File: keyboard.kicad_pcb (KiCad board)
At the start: 2 copper layers, 359.9 x 94.6 mm, 211 parts, among them IC1 ATMEGA32U4, J1 USB C, X1 ASX3F

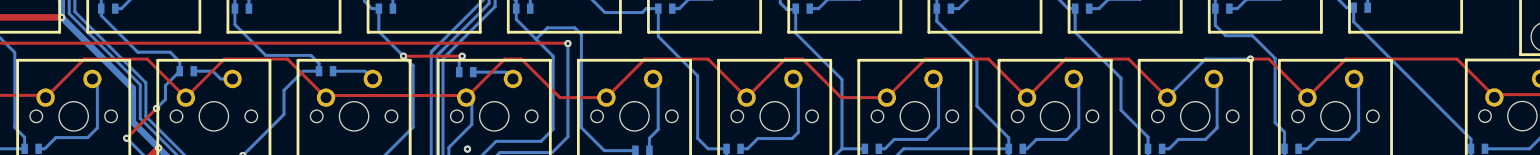
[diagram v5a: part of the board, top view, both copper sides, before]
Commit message: Make fourth row linear
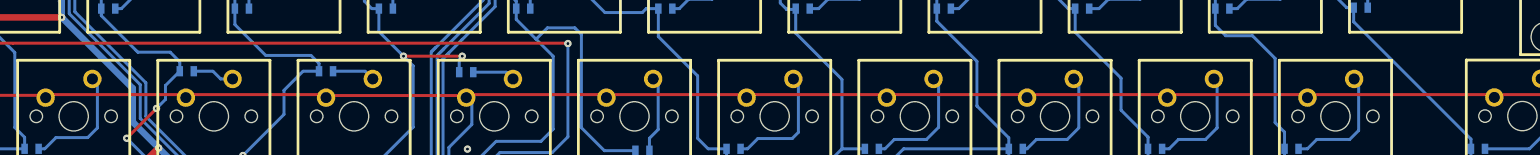
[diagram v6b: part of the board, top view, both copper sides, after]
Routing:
- net /row4: track 410.0 -> 374.6 mm, vias 1 -> 0
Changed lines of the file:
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@@
     (thickness 1.6002)
     (drawings 87)
-    (tracks 1713)
+    (tracks 1718)
     (zones 0)
     (modules 211)
@@
   (layers
     (0 F.Cu signal)
-    (31 B.Cu signal hide)
+    (31 B.Cu signal)
     (32 B.Adhes user hide)
     (33 F.Adhes user hide)
@@
   (segment (start 322.0085 108.966) (end 322.42125 109.37875) (width 0.4064) (layer F.Cu) (net 73))
   (segment (start 291.846 108.966) (end 322.0085 108.966) (width 0.4064) (layer F.Cu) (net 73))
-  (segment (start 191.93002 123.19) (end 186.69 128.43002) (width 0.4064) (layer F.Cu) (net 74))
-  (segment (start 200.49998 123.19) (end 191.93002 123.19) (width 0.4064) (layer F.Cu) (net 74))
-  (segment (start 205.74 128.43002) (end 200.49998 123.19) (width 0.4064) (layer F.Cu) (net 74) (status 10))
-  (segment (start 148.59 128.43002) (end 143.34998 123.19) (width 0.4064) (layer F.Cu) (net 74))
-  (segment (start 124.29998 123.19) (end 115.73002 123.19) (width 0.4064) (layer F.Cu) (net 74))
-  (segment (start 230.03002 123.19) (end 224.79 128.43002) (width 0.4064) (layer F.Cu) (net 74))
-  (segment (start 243.84 128.43002) (end 238.59998 123.19) (width 0.4064) (layer F.Cu) (net 74))
-  (segment (start 238.59998 123.19) (end 230.03002 123.19) (width 0.4064) (layer F.Cu) (net 74))
-  (segment (start 262.89 128.43002) (end 257.64998 123.19) (width 0.4064) (layer F.Cu) (net 74))
-  (segment (start 134.78002 123.19) (end 129.54 128.43002) (width 0.4064) (layer F.Cu) (net 74))
-  (segment (start 129.54 128.43002) (end 124.29998 123.19) (width 0.4064) (layer F.Cu) (net 74))
-  (segment (start 115.73002 123.19) (end 110.49 128.43002) (width 0.4064) (layer F.Cu) (net 74))
-  (segment (start 249.08002 123.19) (end 243.84 128.43002) (width 0.4064) (layer F.Cu) (net 74))
-  (segment (start 143.34998 123.19) (end 134.78002 123.19) (width 0.4064) (layer F.Cu) (net 74))
-  (segment (start 257.64998 123.19) (end 249.08002 123.19) (width 0.4064) (layer F.Cu) (net 74))
-  (segment (start 167.64 128.43002) (end 172.86351 123.20651) (width 0.4064) (layer F.Cu) (net 74))
-  (segment (start 172.86351 123.20651) (end 172.88002 123.19) (width 0.4064) (layer F.Cu) (net 74))
-  (segment (start 180.37302 128.43002) (end 186.69 128.43002) (width 0.4064) (layer F.Cu) (net 74))
-  (segment (start 175.133 123.19) (end 180.37302 128.43002) (width 0.4064) (layer F.Cu) (net 74))
-  (segment (start 172.88002 123.19) (end 175.133 123.19) (width 0.4064) (layer F.Cu) (net 74))
   (segment (start 168.19626 129.18694) (end 167.64 128.43002) (width 0.4064) (layer B.Cu) (net 74))
   (segment (start 78.96225 127.889) (end 79.502 128.42875) (width 0.4064) (layer B.Cu) (net 74))
   (segment (start 79.502 128.42875) (end 79.53375 128.42875) (width 0.4064) (layer B.Cu) (net 74))
-  (segment (start 262.89 128.397) (end 268.097 123.19) (width 0.4064) (layer B.Cu) (net 74))
-  (segment (start 268.097 123.19) (end 274.193 123.19) (width 0.4064) (layer B.Cu) (net 74))
-  (via (at 274.193 123.19) (size 1) (layers F.Cu B.Cu) (net 74))
-  (segment (start 274.193 123.19) (end 276.69998 123.19) (width 0.4064) (layer F.Cu) (net 74))
-  (segment (start 276.69998 123.19) (end 281.94 128.43002) (width 0.4064) (layer F.Cu) (net 74))
   (segment (start 262.89 128.43002) (end 262.89 128.397) (width 0.4064) (layer B.Cu) (net 74))
   (segment (start 167.64 128.43002) (end 168.148 128.93802) (width 0.4064) (layer B.Cu) (net 74))
-  (segment (start 213.36 123.19) (end 218.60002 128.43002) (width 0.4064) (layer F.Cu) (net 74))
-  (segment (start 218.60002 128.43002) (end 224.79 128.43002) (width 0.4064) (layer F.Cu) (net 74))
-  (segment (start 205.74 128.43002) (end 210.98002 123.19) (width 0.4064) (layer F.Cu) (net 74) (status 20))
-  (segment (start 210.98002 123.19) (end 213.36 123.19) (width 0.4064) (layer F.Cu) (net 74))
-  (segment (start 281.94 128.43002) (end 287.18002 123.19) (width 0.4064) (layer F.Cu) (net 74))
-  (segment (start 302.26 123.19) (end 307.34 128.27) (width 0.4064) (layer F.Cu) (net 74))
-  (segment (start 287.18002 123.19) (end 302.26 123.19) (width 0.4064) (layer F.Cu) (net 74))
   (segment (start 307.975 127.635) (end 307.34 128.27) (width 0.4064) (layer F.Cu) (net 74))
   (segment (start 332.74 127.635) (end 333.375 128.27) (width 0.4064) (layer F.Cu) (net 74))
@@
   (segment (start 110.17758 128.1176) (end 110.49 128.43002) (width 0.4064) (layer F.Cu) (net 74))
   (segment (start 79.8576 128.1176) (end 110.17758 128.1176) (width 0.4064) (layer F.Cu) (net 74))
+  (segment (start 110.49 128.43002) (end 110.58398 128.43002) (width 0.4064) (layer F.Cu) (net 74))
+  (segment (start 110.58398 128.43002) (end 110.998 128.016) (width 0.4064) (layer F.Cu) (net 74))
+  (segment (start 129.12598 128.016) (end 129.54 128.43002) (width 0.4064) (layer F.Cu) (net 74))
+  (segment (start 110.998 128.016) (end 129.12598 128.016) (width 0.4064) (layer F.Cu) (net 74))
+  (segment (start 129.54 128.43002) (end 129.54 128.27) (width 0.4064) (layer F.Cu) (net 74))
+  (segment (start 129.54 128.27) (end 129.794 128.016) (width 0.4064) (layer F.Cu) (net 74))
+  (segment (start 148.17598 128.016) (end 148.59 128.43002) (width 0.4064) (layer F.Cu) (net 74))
+  (segment (start 129.794 128.016) (end 148.17598 128.016) (width 0.4064) (layer F.Cu) (net 74))
+  (segment (start 167.64 128.43002) (end 167.64 128.27) (width 0.4064) (layer F.Cu) (net 74))
+  (segment (start 167.64 128.27) (end 167.894 128.016) (width 0.4064) (layer F.Cu) (net 74))
+  (segment (start 186.27598 128.016) (end 186.69 128.43002) (width 0.4064) (layer F.Cu) (net 74))
+  (segment (start 167.894 128.016) (end 186.27598 128.016) (width 0.4064) (layer F.Cu) (net 74))
+  (segment (start 186.69 128.43002) (end 186.78398 128.43002) (width 0.4064) (layer F.Cu) (net 74))
+  (segment (start 186.78398 128.43002) (end 187.198 128.016) (width 0.4064) (layer F.Cu) (net 74))
+  (segment (start 205.32598 128.016) (end 205.74 128.43002) (width 0.4064) (layer F.Cu) (net 74))
+  (segment (start 187.198 128.016) (end 205.32598 128.016) (width 0.4064) (layer F.Cu) (net 74))
+  (segment (start 205.74 128.43002) (end 205.74 128.27) (width 0.4064) (layer F.Cu) (net 74))
+  (segment (start 205.74 128.27) (end 205.994 128.016) (width 0.4064) (layer F.Cu) (net 74))
+  (segment (start 224.37598 128.016) (end 224.79 128.43002) (width 0.4064) (layer F.Cu) (net 74))
+  (segment (start 205.994 128.016) (end 224.37598 128.016) (width 0.4064) (layer F.Cu) (net 74))
+  (segment (start 224.79 128.43002) (end 225.13798 128.43002) (width 0.4064) (layer F.Cu) (net 74))
+  (segment (start 225.13798 128.43002) (end 225.552 128.016) (width 0.4064) (layer F.Cu) (net 74))
+  (segment (start 243.42598 128.016) (end 243.84 128.43002) (width 0.4064) (layer F.Cu) (net 74))
+  (segment (start 225.552 128.016) (end 243.42598 128.016) (width 0.4064) (layer F.Cu) (net 74))
+  (segment (start 243.84 128.43002) (end 244.18798 128.43002) (width 0.4064) (layer F.Cu) (net 74))
+  (segment (start 244.18798 128.43002) (end 244.602 128.016) (width 0.4064) (layer F.Cu) (net 74))
+  (segment (start 262.47598 128.016) (end 262.89 128.43002) (width 0.4064) (layer F.Cu) (net 74))
+  (segment (start 244.602 128.016) (end 262.47598 128.016) (width 0.4064) (layer F.Cu) (net 74))
+  (segment (start 262.89 128.43002) (end 262.98398 128.43002) (width 0.4064) (layer F.Cu) (net 74))
+  (segment (start 262.89 128.43002) (end 263.23798 128.43002) (width 0.4064) (layer F.Cu) (net 74))
+  (segment (start 263.23798 128.43002) (end 263.652 128.016) (width 0.4064) (layer F.Cu) (net 74))
+  (segment (start 281.52598 128.016) (end 281.94 128.43002) (width 0.4064) (layer F.Cu) (net 74))
+  (segment (start 263.652 128.016) (end 281.52598 128.016) (width 0.4064) (layer F.Cu) (net 74))
+  (segment (start 281.94 128.43002) (end 281.94 128.27) (width 0.4064) (layer F.Cu) (net 74))
+  (segment (start 281.94 128.27) (end 282.194 128.016) (width 0.4064) (layer F.Cu) (net 74))
+  (segment (start 306.959 128.016) (end 307.34 128.397) (width 0.4064) (layer F.Cu) (net 74))
+  (segment (start 282.194 128.016) (end 306.959 128.016) (width 0.4064) (layer F.Cu) (net 74))
   (segment (start 93.853 147.447) (end 93.82125 147.47875) (width 0.4064) (layer F.Cu) (net 75))
   (segment (start 117.221 147.066) (end 117.63375 147.47875) (width 0.4064) (layer F.Cu) (net 75))

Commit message: Tidy up columns
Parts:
- moved D10 11.3 mm to (105.9, 146.8)
- moved C8 4.35 mm to (74.2, 83.1)
- moved D3 1.85 mm to (70.1, 115.8)
- moved D1 1.34 mm to (67.9, 86.9)
- moved D33 0.25 mm to (194.7, 116.6)
- moved D5 0.20 mm to (68.1, 143.6)
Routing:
- net /col2: track 162.4 -> 144.6 mm
- net Net-(IC1-Pad4): track 116.6 -> 124.0 mm
- net /col14: track 303.5 -> 310.7 mm
- net /col1: track 170.8 -> 165.7 mm
- net Net-(D66-Pad2): track 19.9 -> 15.8 mm
- net Net-(D10-Pad2): track 4.68 -> 8.30 mm
- net VCC: track 912.6 -> 909.1 mm
- net Net-(D18-Pad2): track 13.2 -> 16.7 mm
- net Net-(D23-Pad2): track 19.6 -> 16.3 mm
- net Net-(D58-Pad2): track 19.7 -> 17.2 mm
- net Net-(D3-Pad2): track 20.8 -> 18.4 mm
- net /col11: track 229.3 -> 227.2 mm
- net Net-(D28-Pad2): track 20.9 -> 19.3 mm
- net Net-(D13-Pad2): track 14.4 -> 15.9 mm
- net Net-(D33-Pad2): track 15.8 -> 17.1 mm
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
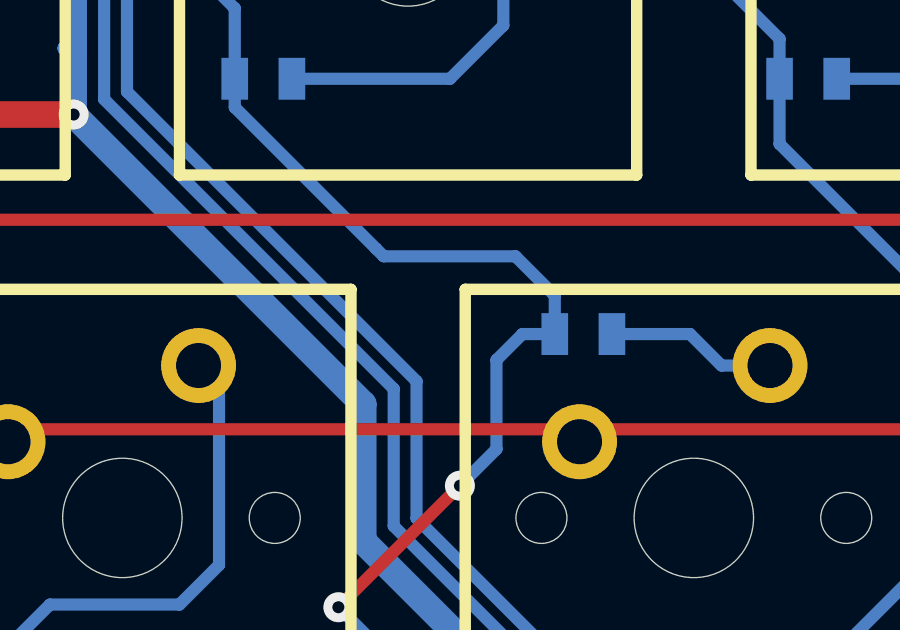
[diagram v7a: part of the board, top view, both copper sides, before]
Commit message: Add ground via
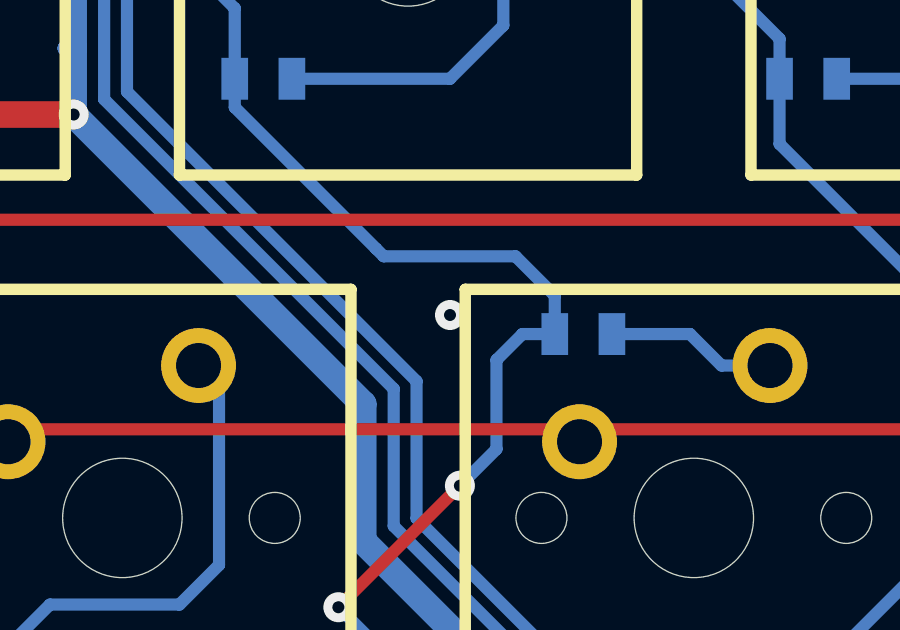
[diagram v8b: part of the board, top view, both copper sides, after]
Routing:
- net GND: vias 11 -> 12
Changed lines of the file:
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@@
     (thickness 1.6002)
     (drawings 87)
-    (tracks 1684)
+    (tracks 1685)
     (zones 0)
     (modules 211)
@@
   (via (at 167.80764 135.42264) (size 1) (drill 0.4) (layers F.Cu B.Cu) (net 1))
   (via (at 147.701 141.86916) (size 1) (drill 0.4) (layers F.Cu B.Cu) (net 1))
+  (via (at 125.222 124.206) (size 1) (drill 0.4) (layers F.Cu B.Cu) (net 1))
   (segment (start 155.56992 144.90954) (end 155.57246 144.907) (width 0.4064) (layer B.Cu) (net 2))
   (segment (start 83.48726 84.75726) (end 87.503 84.75726) (width 0.889) (layer B.Cu) (net 2))
